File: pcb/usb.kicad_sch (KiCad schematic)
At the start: 25 parts, among them J6 USB4105, J7 Conn_01x02, Q1 DMG3401LSN, Q2 DMG3418L, Q3 DMG3418L, SW1 PBH2UEESNPNAGX, U149 SN74LVC2G132DCUR, U151 AP2112K-3.3, U152 BQ297xy, U153 MCP73831-2-OT

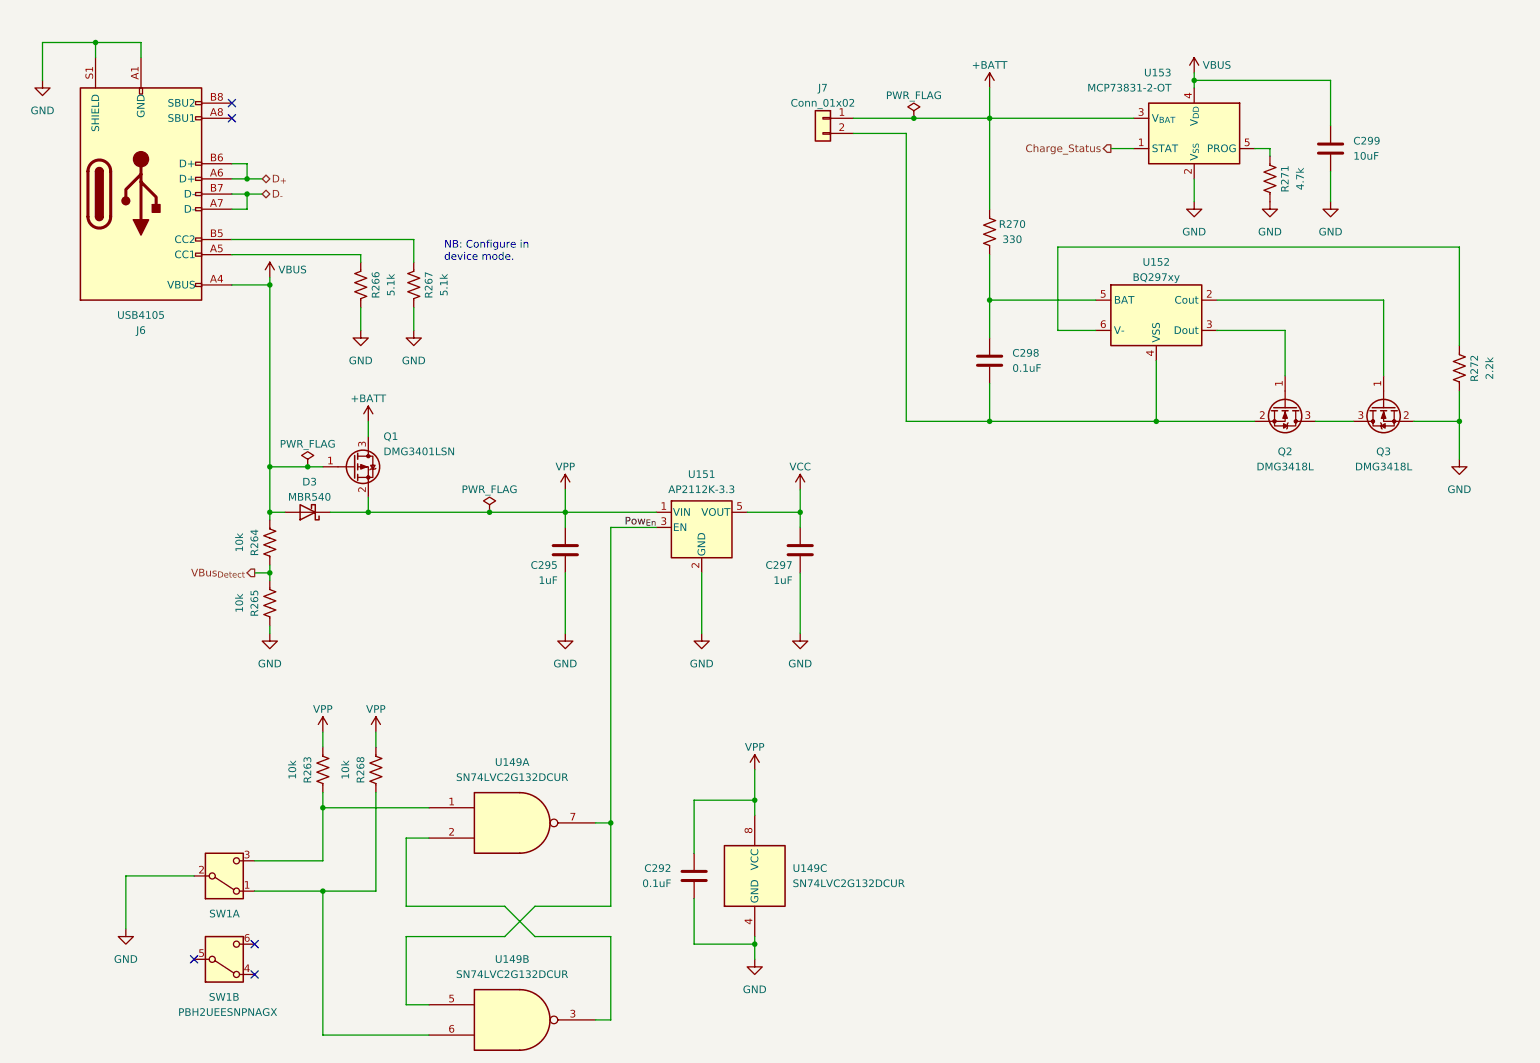
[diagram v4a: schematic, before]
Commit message: Initial Rev. A schematic
- I think this has everything we need for revision A
- Battery charge indication via the OLED display
- User interface via rotary encoder/select switch
- Cycle through affected individual channels, none, or all
- Cycle through amplitudes
- Cycle through frequencies
- Select signal source
- Cycle through pre-loaded channel maps?
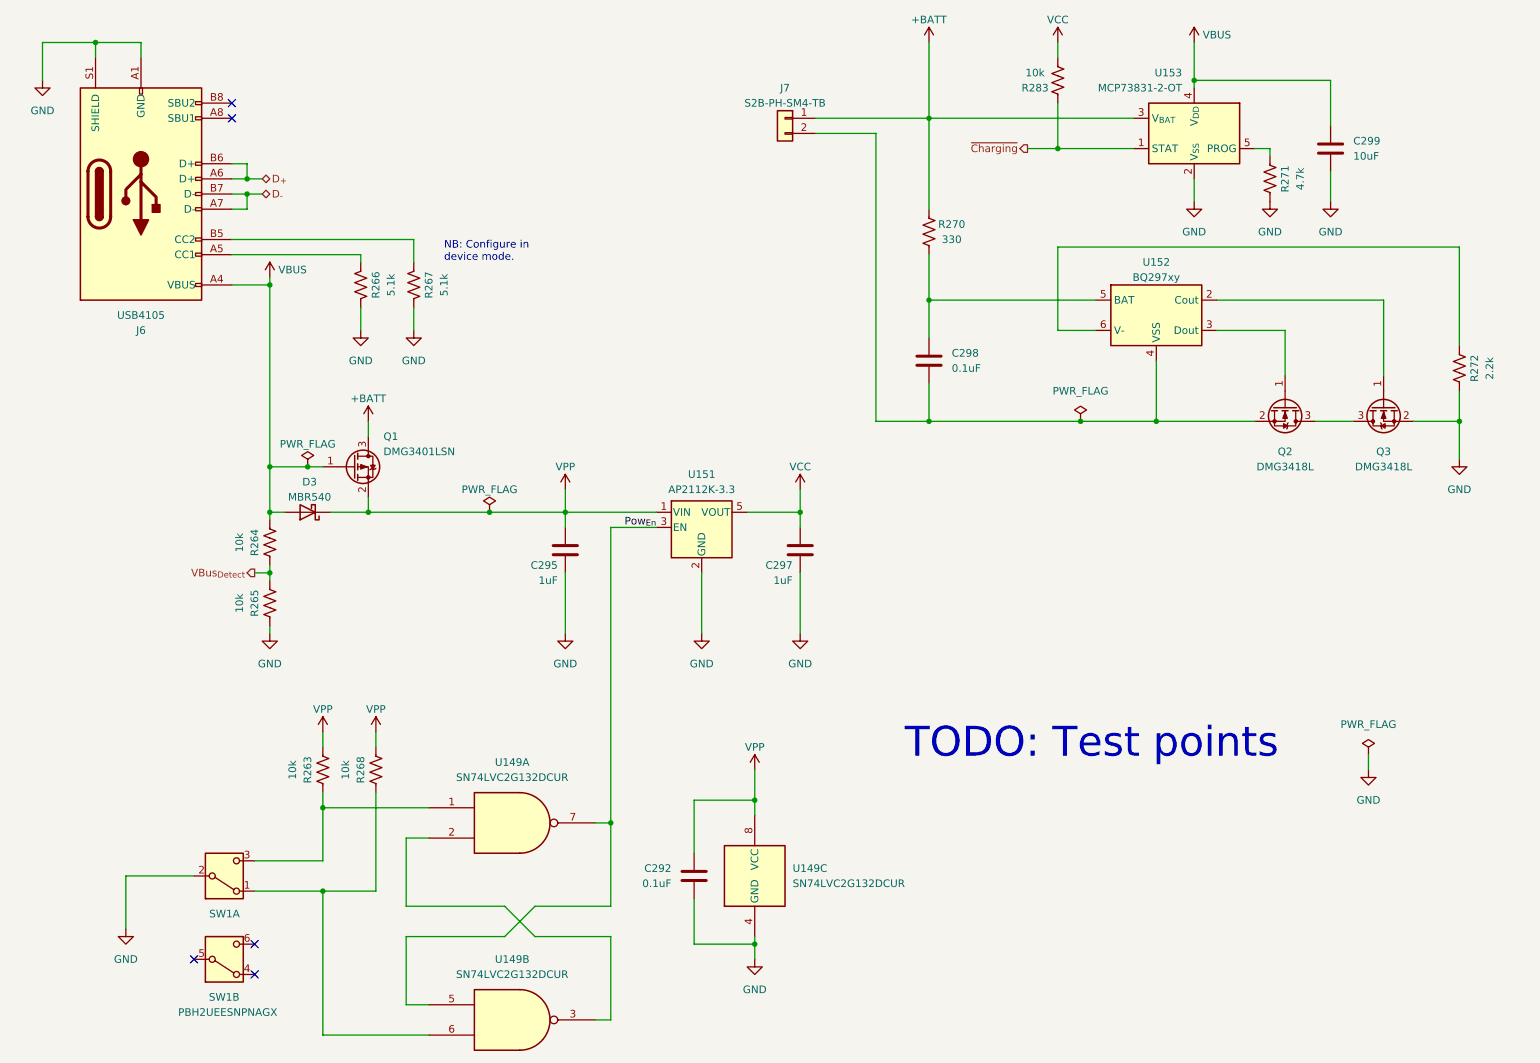
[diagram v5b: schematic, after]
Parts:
- added R283: 10k, Resistor_SMD:R_0402_1005Metric, symbol Device:R_US
- J7: value Conn_01x02 -> S2B-PH-SM4-TB
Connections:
- net VCC: now also R283.1
- net Charge_Status renamed ~{Charging}
- net ~{Charging}: now also R283.2
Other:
- note added: "TODO: Test points"
- moved on the sheet: C298, J7, R270

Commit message: More schematic improvements
- Add pullups to i2c bus
- Add test points
- Ready for initial routing
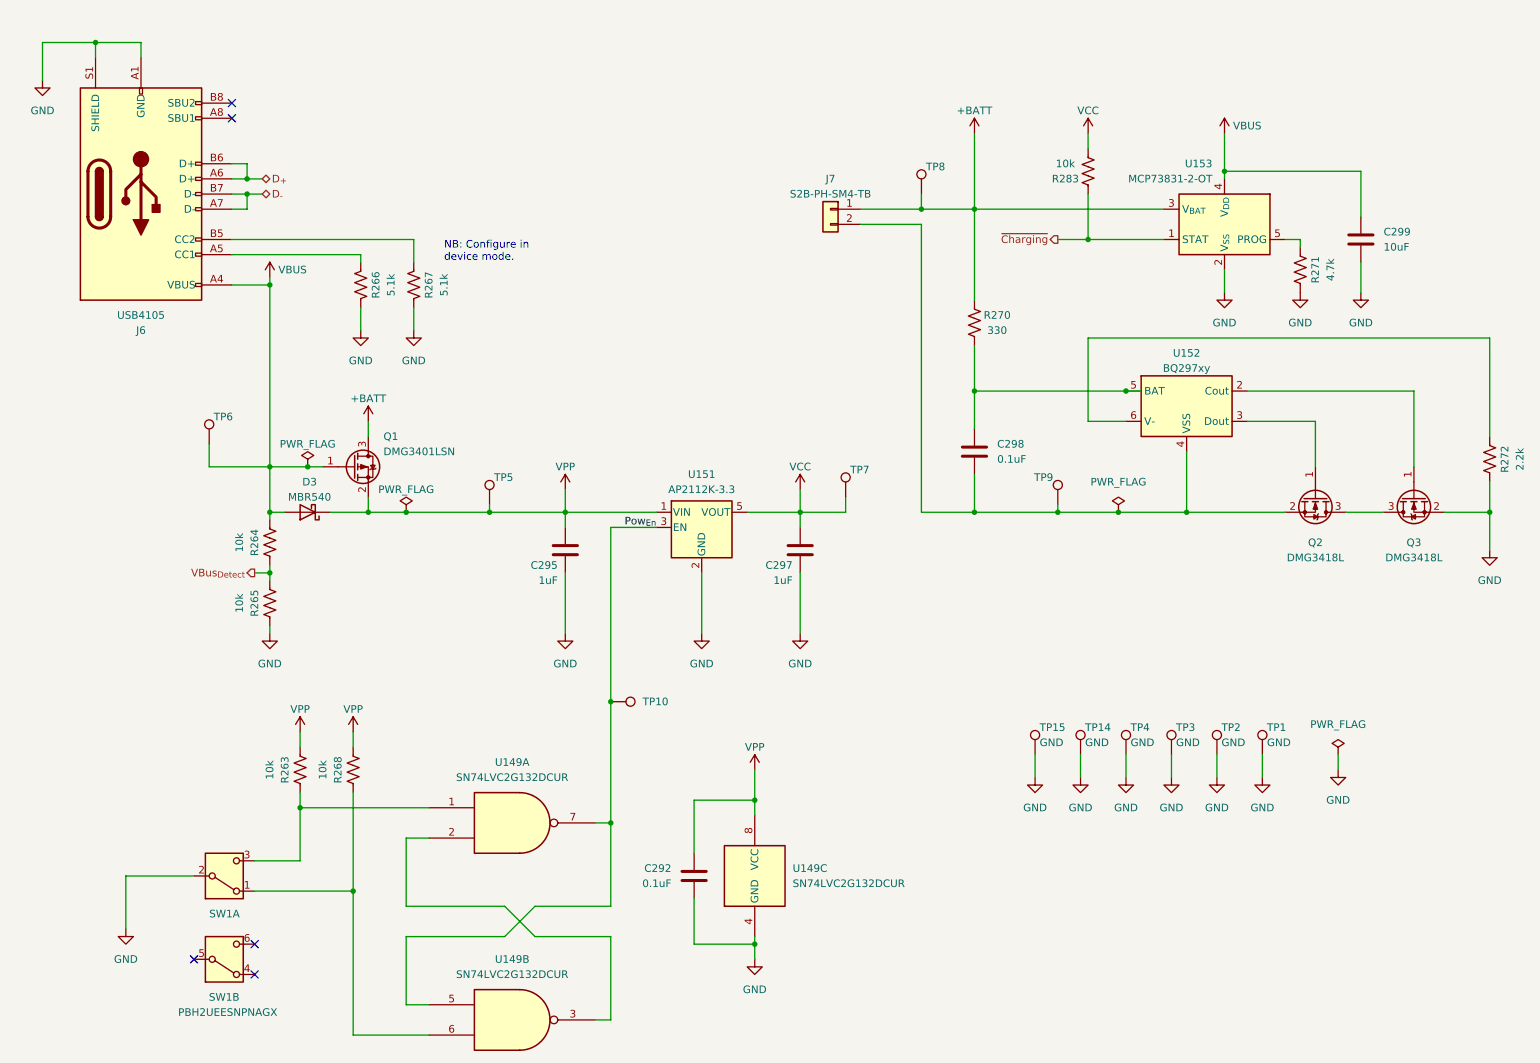
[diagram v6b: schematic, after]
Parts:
- added TP1, TP10, TP14, TP15, TP2, TP3, TP4, TP5, TP6, TP8, TP9: GND, TestPoint:TestPoint_Pad_D2.0mm, symbol Connector:TestPoint
- added TP7: VCC, TestPoint:TestPoint_Pad_D2.0mm, symbol Connector:TestPoint
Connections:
- net +BATT: now also TP8.1
- net GND: now also TP1.1, TP14.1, TP15.1, TP2.1, TP3.1, TP4.1
- net Pow_{En}: now also TP10.1
- net VBUS: now also TP6.1
- net VCC: now also TP7.1
- net VPP: now also TP5.1
- net at C298.2, J7.2 (Pin_2), Q2.2 (S)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: now also TP9.1
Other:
- note removed: "TODO: Test points"
- moved on the sheet: C298, C299, J7, Q2, Q3, R263, R268, R270, R271, R272, R283, U152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

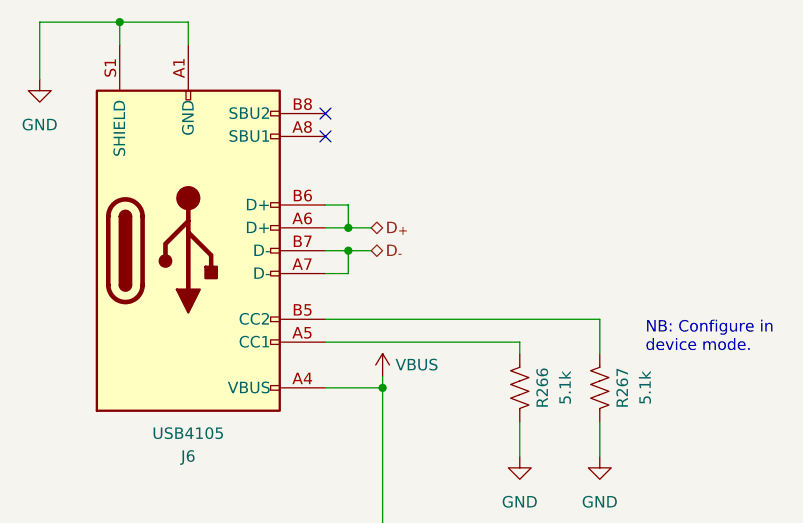
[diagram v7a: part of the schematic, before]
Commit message: Routing nearly complete
- Power switch is too tall I think
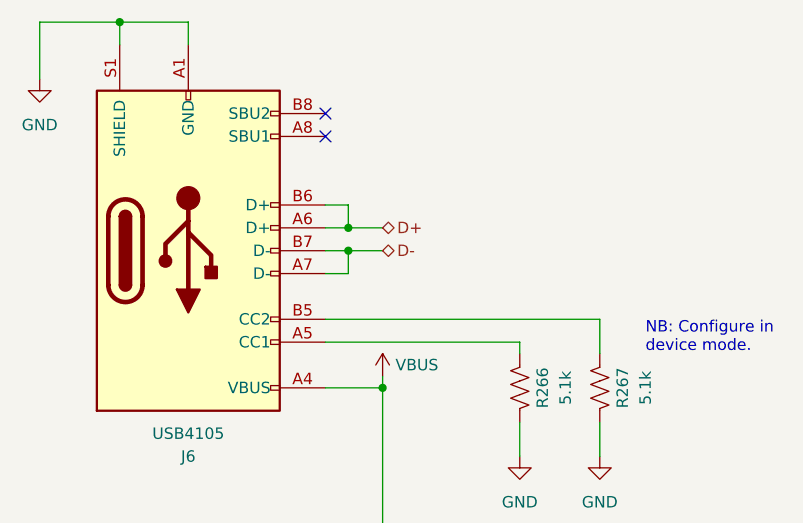
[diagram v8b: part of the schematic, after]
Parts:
- C292, C298: TempCo (none) -> X7R
- C295, C297: TempCo (none) -> X5R; Voltage (none) -> 16V
- C299: footprint Capacitor_SMD:C_0805_2012Metric -> Capacitor_SMD:C_1206_3216Metric; TempCo (none) -> X5R; Voltage (none) -> 16V
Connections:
- net D_{+} renamed D+
- net D_{-} renamed D-
